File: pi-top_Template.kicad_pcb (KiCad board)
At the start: 2 copper layers, 65 x 56 mm, 6 parts, among them J1 3M 951 Series, J2 Harwin M22-655R

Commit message: Still shuffling files around
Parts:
- removed M** (x4): MountingHole_2.5mm_Pad, Mounting_Holes:MountingHole_2.5mm_Pad
- added REF**: MountingHole_2.7mm_M2.5_ISO7380_Pad, Mounting_Holes:MountingHole_2.7mm_M2.5_ISO7380_Pad, F.Cu at (99.5, 126.5)
- added REF**: MountingHole_2.7mm_M2.5_ISO7380_Pad, Mounting_Holes:MountingHole_2.7mm_M2.5_ISO7380_Pad, F.Cu at (41.5, 126.5)
- added REF**: MountingHole_2.7mm_M2.5_ISO7380_Pad, Mounting_Holes:MountingHole_2.7mm_M2.5_ISO7380_Pad, F.Cu at (99.5, 77.5)
- added REF**: MountingHole_2.7mm_M2.5_ISO7380_Pad, Mounting_Holes:MountingHole_2.7mm_M2.5_ISO7380_Pad, F.Cu at (41.5, 77.5)
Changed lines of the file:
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@@
     (links 34)
     (no_connects 34)
-    (area 30.067857 66.300001 119.49643 136.700001)
+    (area 25.844048 66.300001 119.49643 136.700001)
     (thickness 1.6)
     (drawings 25)
@@
     (mod_text_size 1 1)
     (mod_text_width 0.15)
-    (pad_size 5 5)
-    (pad_drill 2.5)
+    (pad_size 4.5 4.5)
+    (pad_drill 2.7)
     (pad_to_mask_clearance 0.2)
     (aux_axis_origin 0 0)
+    (grid_origin 38 74)
     (visible_elements 7FFFF77F)
     (pcbplotparams
@@
     (add_net SPDIF_OUT)
     (add_net TXD_BCM-15)
+  )
+  (module Mounting_Holes:MountingHole_2.7mm_M2.5_ISO7380_Pad locked (layer F.Cu)
+    (at 99.5 126.5)
+    (descr "Mounting Hole 2.7mm, M2.5, ISO7380")
+    (tags "mounting hole 2.7mm m2.5 iso7380")
+    (fp_text reference REF** (at 0 -3.25) (layer F.SilkS) hide
+      (effects (font (size 1 1) (thickness 0.15)))
+    )
+    (fp_text value MountingHole_2.7mm_M2.5_ISO7380_Pad (at 0 3.25) (layer F.Fab) hide
+      (effects (font (size 1 1) (thickness 0.15)))
+    )
+    (fp_circle (center 0 0) (end 2.25 0) (layer Cmts.User) (width 0.15))
+    (fp_circle (center 0 0) (end 2.5 0) (layer F.CrtYd) (width 0.05))
+    (pad 3 thru_hole circle (at 0 0) (size 4.5 4.5) (drill 2.7) (layers *.Cu *.Mask))
+  )
+  (module Mounting_Holes:MountingHole_2.7mm_M2.5_ISO7380_Pad locked (layer F.Cu)
+    (at 41.5 126.5)
+    (descr "Mounting Hole 2.7mm, M2.5, ISO7380")
+    (tags "mounting hole 2.7mm m2.5 iso7380")
+    (fp_text reference REF** (at 0 -3.25) (layer F.SilkS) hide
+      (effects (font (size 1 1) (thickness 0.15)))
+    )
+    (fp_text value MountingHole_2.7mm_M2.5_ISO7380_Pad (at 0 3.25) (layer F.Fab) hide
+      (effects (font (size 1 1) (thickness 0.15)))
+    )
+    (fp_circle (center 0 0) (end 2.25 0) (layer Cmts.User) (width 0.15))
+    (fp_circle (center 0 0) (end 2.5 0) (layer F.CrtYd) (width 0.05))
+    (pad 4 thru_hole circle (at 0 0) (size 4.5 4.5) (drill 2.7) (layers *.Cu *.Mask))
+  )
+  (module Mounting_Holes:MountingHole_2.7mm_M2.5_ISO7380_Pad locked (layer F.Cu)
+    (at 99.5 77.5)
+    (descr "Mounting Hole 2.7mm, M2.5, ISO7380")
+    (tags "mounting hole 2.7mm m2.5 iso7380")
+    (fp_text reference REF** (at 0 -3.25) (layer F.SilkS) hide
+      (effects (font (size 1 1) (thickness 0.15)))
+    )
+    (fp_text value MountingHole_2.7mm_M2.5_ISO7380_Pad (at 0 3.25) (layer F.Fab) hide
+      (effects (font (size 1 1) (thickness 0.15)))
+    )
+    (fp_circle (center 0 0) (end 2.25 0) (layer Cmts.User) (width 0.15))
+    (fp_circle (center 0 0) (end 2.5 0) (layer F.CrtYd) (width 0.05))
+    (pad 2 thru_hole circle (at 0 0) (size 4.5 4.5) (drill 2.7) (layers *.Cu *.Mask))
+  )
+  (module Mounting_Holes:MountingHole_2.7mm_M2.5_ISO7380_Pad locked (layer F.Cu)
+    (at 41.5 77.5)
+    (descr "Mounting Hole 2.7mm, M2.5, ISO7380")
+    (tags "mounting hole 2.7mm m2.5 iso7380")
+    (fp_text reference REF** (at 0 -3.25) (layer F.SilkS) hide
+      (effects (font (size 1 1) (thickness 0.15)))
+    )
+    (fp_text value MountingHole_2.7mm_M2.5_ISO7380_Pad (at 0 3.25) (layer F.Fab) hide
+      (effects (font (size 1 1) (thickness 0.15)))
+    )
+    (fp_circle (center 0 0) (end 2.25 0) (layer Cmts.User) (width 0.15))
+    (fp_circle (center 0 0) (end 2.5 0) (layer F.CrtYd) (width 0.05))
+    (pad 1 thru_hole circle (at 0 0) (size 4.5 4.5) (drill 2.7) (layers *.Cu *.Mask))
   )
   (module library:3M_951217-4620-XX (layer B.Cu)
@@
       (net 1 BCM-24))
   )
-  (module Mounting_Holes:MountingHole_2.5mm_Pad locked (layer F.Cu)
-    (at 41.5 77.5)
-    (descr "Mounting Hole 2.5mm")
-    (tags "mounting hole 2.5mm")
-    (fp_text reference M** (at 0 -3.5) (layer F.SilkS) hide
-      (effects (font (size 1 1) (thickness 0.15)))
-    )
-    (fp_text value MountingHole_2.5mm_Pad (at 0 3.5) (layer F.Fab) hide
-      (effects (font (size 1 1) (thickness 0.15)))
-    )
-    (fp_circle (center 0 0) (end 2.5 0) (layer Cmts.User) (width 0.15))
-    (fp_circle (center 0 0) (end 2.75 0) (layer F.CrtYd) (width 0.05))
-    (pad 1 thru_hole circle (at 0 0) (size 5 5) (drill 2.5) (layers *.Cu *.Mask))
-  )
-  (module Mounting_Holes:MountingHole_2.5mm_Pad locked (layer F.Cu)
-    (at 99.5 77.5)
-    (descr "Mounting Hole 2.5mm")
-    (tags "mounting hole 2.5mm")
-    (fp_text reference M** (at 0 -3.5) (layer F.SilkS) hide
-      (effects (font (size 1 1) (thickness 0.15)))
-    )
-    (fp_text value MountingHole_2.5mm_Pad (at 0 3.5) (layer F.Fab) hide
-      (effects (font (size 1 1) (thickness 0.15)))
-    )
-    (fp_circle (center 0 0) (end 2.5 0) (layer Cmts.User) (width 0.15))
-    (fp_circle (center 0 0) (end 2.75 0) (layer F.CrtYd) (width 0.05))
-    (pad 2 thru_hole circle (at 0 0) (size 5 5) (drill 2.5) (layers *.Cu *.Mask))
-  )
-  (module Mounting_Holes:MountingHole_2.5mm_Pad locked (layer F.Cu)
-    (at 99.5 126.5)
-    (descr "Mounting Hole 2.5mm")
-    (tags "mounting hole 2.5mm")
-    (fp_text reference M** (at 0 -3.5) (layer F.SilkS) hide
-      (effects (font (size 1 1) (thickness 0.15)))
-    )
-    (fp_text value MountingHole_2.5mm_Pad (at 0 3.5) (layer F.Fab) hide
-      (effects (font (size 1 1) (thickness 0.15)))
-    )
-    (fp_circle (center 0 0) (end 2.5 0) (layer Cmts.User) (width 0.15))
-    (fp_circle (center 0 0) (end 2.75 0) (layer F.CrtYd) (width 0.05))
-    (pad 3 thru_hole circle (at 0 0) (size 5 5) (drill 2.5) (layers *.Cu *.Mask))
-  )
-  (module Mounting_Holes:MountingHole_2.5mm_Pad locked (layer F.Cu)
-    (at 41.5 126.5)
-    (descr "Mounting Hole 2.5mm")
-    (tags "mounting hole 2.5mm")
-    (fp_text reference M** (at 0 -3.5) (layer F.SilkS) hide
-      (effects (font (size 1 1) (thickness 0.15)))
-    )
-    (fp_text value MountingHole_2.5mm_Pad (at 0 3.5) (layer F.Fab) hide
-      (effects (font (size 1 1) (thickness 0.15)))
-    )
-    (fp_circle (center 0 0) (end 2.5 0) (layer Cmts.User) (width 0.15))
-    (fp_circle (center 0 0) (end 2.75 0) (layer F.CrtYd) (width 0.05))
-    (pad 4 thru_hole circle (at 0 0) (size 5 5) (drill 2.5) (layers *.Cu *.Mask))
-  )
   (module library:Harwin_M22-6553442R locked (layer B.Cu)

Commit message: Added 3D models to connectors
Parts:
- J1: footprint library:3M_951217-4620-XX -> pi-top:3M_951217-4620-XX
- J2: footprint library:Harwin_M22-6553442R -> pi-top:Harwin_M22-6553442R

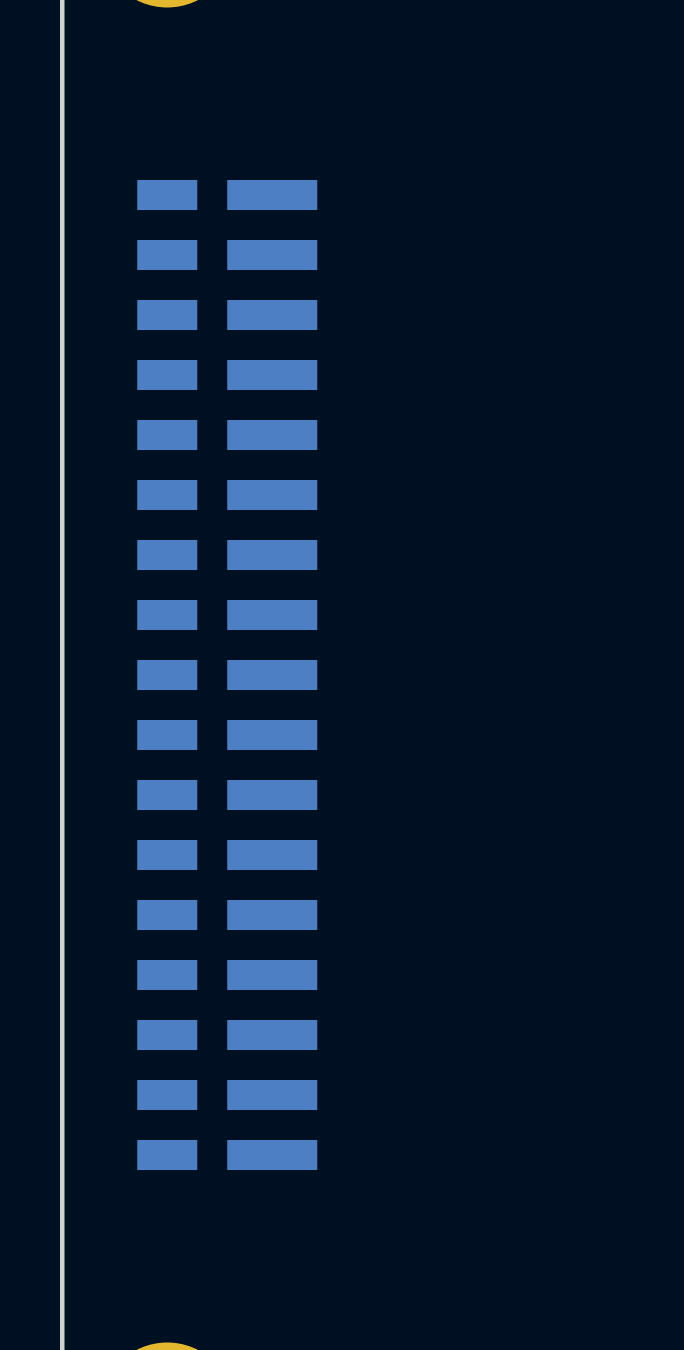
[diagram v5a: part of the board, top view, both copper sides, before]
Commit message: Updated repo name and README to reflect addition of THT version
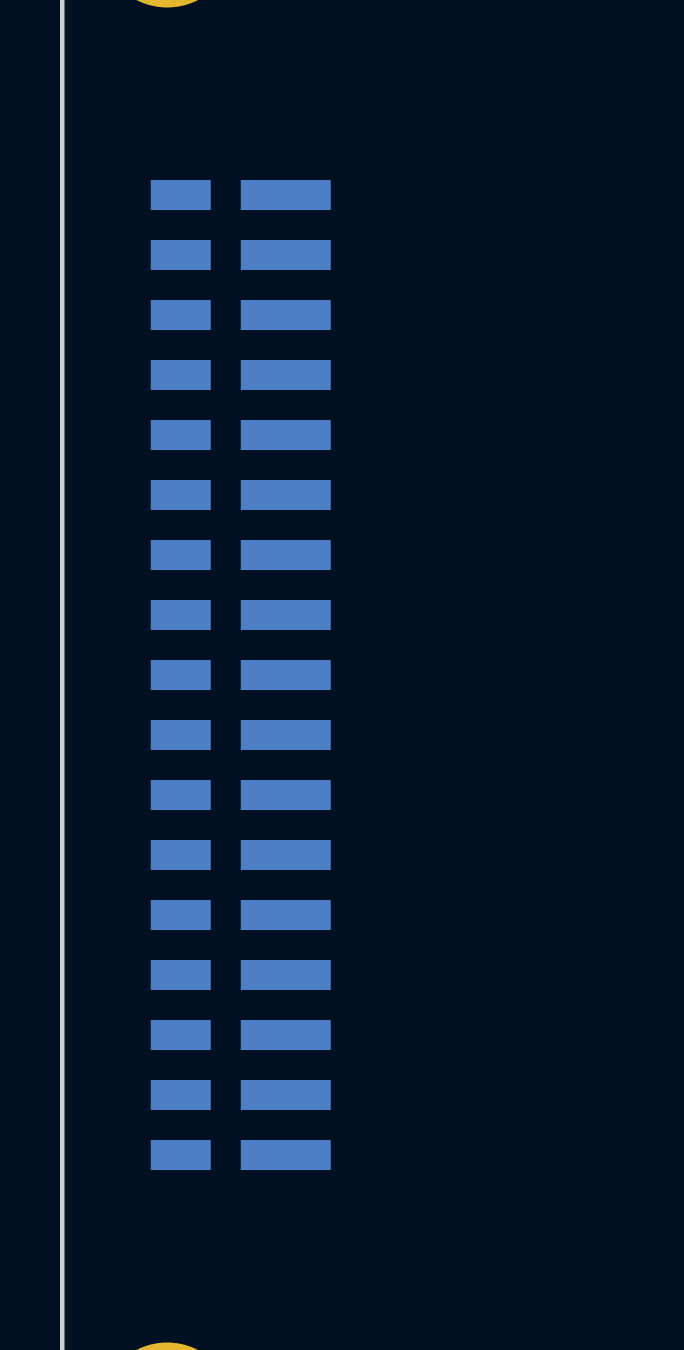
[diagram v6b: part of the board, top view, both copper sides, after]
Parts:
- moved J1 0.45 mm to (43.5, 101.0)
